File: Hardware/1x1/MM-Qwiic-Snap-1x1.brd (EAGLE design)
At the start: 80 x 34.3 mm, 57 parts, among them J15 MICROMOD-2222-C, J2 QWIIC_RIGHT_ANGLE, U1 MCP73831, U5 AP7361C-33FGEUDFN-8

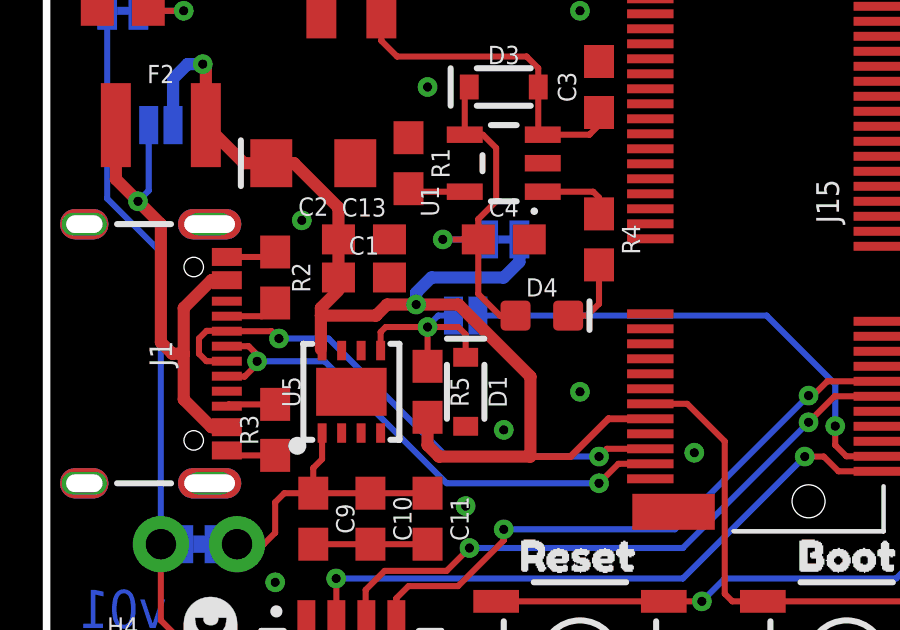
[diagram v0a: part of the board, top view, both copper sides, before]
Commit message: Create 2x1 version and generate production files
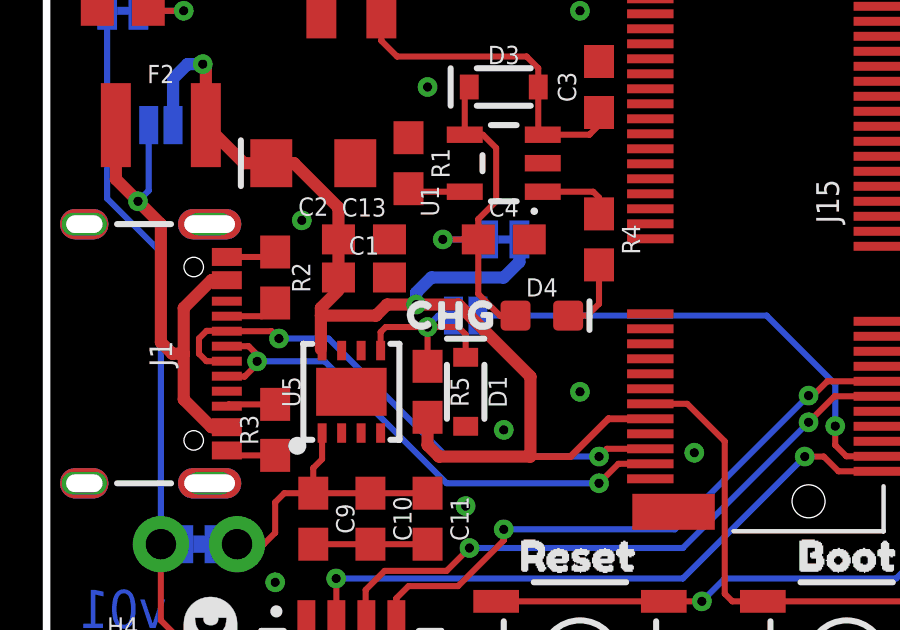
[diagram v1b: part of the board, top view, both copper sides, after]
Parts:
- added U$4: (no value), output:CHG0
- added U$5: (no value), output:#VIN#0
- added U$6: (no value), output:#3#3V#0
- added U$7: (no value), output:#BYP#0
- added U$8: (no value), output:#VE#0
- added U$9: (no value), output:#MEAS#0
- moved LOGO1 7.62 mm to (31.8, 19.1)
- moved LOGO3 7.62 mm to (31.6, 9.65)
- moved U$68 7.62 mm to (31.8, 15.2)
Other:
- board text removed: "Selective Solder Nozzle Width: 0.354331"
- board text removed: "in"
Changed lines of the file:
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@@
 <?xml version="1.0" encoding="utf-8"?>
 <!DOCTYPE eagle SYSTEM "eagle.dtd">
-<eagle version="9.5.2">
+<eagle version="9.6.2">
 <drawing>
 <settings>
@@
 <layer number="23" name="tOrigins" color="15" fill="1" visible="yes" active="yes"/>
 <layer number="24" name="bOrigins" color="15" fill="1" visible="yes" active="yes"/>
-<layer number="25" name="tNames" color="7" fill="1" visible="no" active="yes"/>
-<layer number="26" name="bNames" color="7" fill="1" visible="no" active="yes"/>
-<layer number="27" name="tValues" color="7" fill="1" visible="no" active="yes"/>
-<layer number="28" name="bValues" color="7" fill="1" visible="no" active="yes"/>
-<layer number="29" name="tStop" color="7" fill="3" visible="no" active="yes"/>
-<layer number="30" name="bStop" color="7" fill="6" visible="no" active="yes"/>
-<layer number="31" name="tCream" color="7" fill="4" visible="no" active="yes"/>
-<layer number="32" name="bCream" color="7" fill="5" visible="no" active="yes"/>
-<layer number="33" name="tFinish" color="6" fill="3" visible="no" active="yes"/>
-<layer number="34" name="bFinish" color="6" fill="6" visible="no" active="yes"/>
-<layer number="35" name="tGlue" color="7" fill="4" visible="no" active="yes"/>
-<layer number="36" name="bGlue" color="7" fill="5" visible="no" active="yes"/>
-<layer number="37" name="tTest" color="7" fill="1" visible="no" active="yes"/>
-<layer number="38" name="bTest" color="7" fill="1" visible="no" active="yes"/>
-<layer number="39" name="tKeepout" color="4" fill="11" visible="no" active="yes"/>
-<layer number="40" name="bKeepout" color="1" fill="11" visible="no" active="yes"/>
-<layer number="41" name="tRestrict" color="4" fill="10" visible="no" active="yes"/>
-<layer number="42" name="bRestrict" color="1" fill="10" visible="no" active="yes"/>
-<layer number="43" name="vRestrict" color="2" fill="10" visible="no" active="yes"/>
-<layer number="44" name="Drills" color="7" fill="1" visible="no" active="yes"/>
+<layer number="25" name="tNames" color="7" fill="1" visible="yes" active="yes"/>
+<layer number="26" name="bNames" color="7" fill="1" visible="yes" active="yes"/>
+<layer number="27" name="tValues" color="7" fill="1" visible="yes" active="yes"/>
+<layer number="28" name="bValues" color="7" fill="1" visible="yes" active="yes"/>
+<layer number="29" name="tStop" color="7" fill="3" visible="yes" active="yes"/>
+<layer number="30" name="bStop" color="7" fill="6" visible="yes" active="yes"/>
+<layer number="31" name="tCream" color="7" fill="4" visible="yes" active="yes"/>
+<layer number="32" name="bCream" color="7" fill="5" visible="yes" active="yes"/>
+<layer number="33" name="tFinish" color="6" fill="3" visible="yes" active="yes"/>
+<layer number="34" name="bFinish" color="6" fill="6" visible="yes" active="yes"/>
+<layer number="35" name="tGlue" color="7" fill="4" visible="yes" active="yes"/>
+<layer number="36" name="bGlue" color="7" fill="5" visible="yes" active="yes"/>
+<layer number="37" name="tTest" color="7" fill="1" visible="yes" active="yes"/>
+<layer number="38" name="bTest" color="7" fill="1" visible="yes" active="yes"/>
+<layer number="39" name="tKeepout" color="4" fill="11" visible="yes" active="yes"/>
+<layer number="40" name="bKeepout" color="1" fill="11" visible="yes" active="yes"/>
+<layer number="41" name="tRestrict" color="4" fill="10" visible="yes" active="yes"/>
+<layer number="42" name="bRestrict" color="1" fill="10" visible="yes" active="yes"/>
+<layer number="43" name="vRestrict" color="2" fill="10" visible="yes" active="yes"/>
+<layer number="44" name="Drills" color="7" fill="1" visible="yes" active="yes"/>
 <layer number="45" name="Holes" color="7" fill="1" visible="yes" active="yes"/>
-<layer number="46" name="Milling" color="3" fill="1" visible="no" active="yes"/>
-<layer number="47" name="Measures" color="7" fill="1" visible="no" active="yes"/>
-<layer number="48" name="Document" color="7" fill="1" visible="no" active="yes"/>
-<layer number="49" name="Reference" color="7" fill="1" visible="no" active="yes"/>
-<layer number="50" name="dxf" color="7" fill="1" visible="no" active="yes"/>
+<layer number="46" name="Milling" color="3" fill="1" visible="yes" active="yes"/>
+<layer number="47" name="Measures" color="7" fill="1" visible="yes" active="yes"/>
+<layer number="48" name="Document" color="7" fill="1" visible="yes" active="yes"/>
+<layer number="49" name="Reference" color="7" fill="1" visible="yes" active="yes"/>
+<layer number="50" name="dxf" color="7" fill="1" visible="yes" active="yes"/>
 <layer number="51" name="tDocu" color="6" fill="1" visible="yes" active="yes"/>
-<layer number="52" name="bDocu" color="7" fill="1" visible="no" active="yes"/>
+<layer number="52" name="bDocu" color="7" fill="1" visible="yes" active="yes"/>
 <layer number="91" name="Nets" color="2" fill="1" visible="no" active="no"/>
 <layer number="92" name="Busses" color="1" fill="1" visible="no" active="no"/>
@@
 <wire x1="41.783" y1="47.244" x2="41.783" y2="46.863" width="0.2032" layer="41"/>
 <text x="36.83" y="-21.59" size="1.778" layer="51" font="vector" ratio="15">Priyanka Makin</text>
-<wire x1="58.42" y1="50.8" x2="58.42" y2="40.64" width="9.00000625" layer="48"/>
-<wire x1="58.42" y1="40.64" x2="55.88" y2="35.56" width="9.00000625" layer="48"/>
-<wire x1="55.88" y1="35.56" x2="55.88" y2="12.7" width="9.00000625" layer="48"/>
-<text x="71.12" y="40.64" size="1.778" layer="48" font="vector" ratio="15">Selective Solder Nozzle Width:
-0.354331</text>
-<dimension x1="2.54" y1="55.88" x2="64.77" y2="55.88" x3="33.655" y3="60.96" textsize="1.778" textratio="15" layer="47" unit="inch"/>
-<dimension x1="64.77" y1="55.88" x2="64.77" y2="2.54" x3="74.93" y3="29.21" textsize="1.778" textratio="15" layer="47" unit="inch"/>
-<text x="36.83" y="66.548" size="1.778" layer="47" font="vector" ratio="15">in</text>
-<text x="78.105" y="32.512" size="1.778" layer="47" font="vector" ratio="15" rot="R90">in</text>
-<text x="74.295" y="32.512" size="1.778" layer="47" font="vector" ratio="15" rot="R90">in</text>
-<text x="38.608" y="63.246" size="1.778" layer="47" font="vector" ratio="15" rot="R180">in</text>
-<dimension x1="0" y1="58.42" x2="67.31" y2="58.42" x3="33.655" y3="66.04" textsize="1.778" textratio="15" layer="47" unit="inch"/>
-<dimension x1="67.31" y1="58.42" x2="67.31" y2="0" x3="78.74" y3="29.21" textsize="1.778" textratio="15" layer="47" unit="inch"/>
 </plain>
 <attributes>
@@
 <element name="U$19" library="buzzard_labels (10)" package="BOOT2" value="" x="24.13" y="7.239" smashed="yes"/>
 <element name="LOGO2" library="SparkFun-Aesthetics" package="QWIIC_5.5MM" value="QWIIC_LOGO_CONNECTOR" x="5.461" y="3.1115" smashed="yes" rot="R90"/>
-<element name="LOGO3" library="SparkFun-Aesthetics" package="OSHW-LOGO-M" value="OSHW-LOGOM" x="24.003" y="9.652" smashed="yes" rot="MR0"/>
+<element name="LOGO3" library="SparkFun-Aesthetics" package="OSHW-LOGO-M" value="OSHW-LOGOM" x="31.623" y="9.652" smashed="yes" rot="MR0"/>
 <element name="U$55" library="buzzard_labels (9)" package="22229" value="" x="28.232" y="31.12" smashed="yes"/>
 <element name="H5" library="SparkFun-Hardware" package="STAND-OFF-REFLOW-M2.5" value="STAND-OFF-REFLOW2.5MM_TALL" x="45.47" y="15.03" smashed="yes">
@@
 <attribute name="VALUE" x="24.765" y="19.05" size="0.762" layer="27" rot="R270" align="center"/>
 </element>
-<element name="LOGO1" library="SparkFun-Aesthetics" package="SFE_LOGO_NAME_FLAME_.2" value="SFE_LOGO_NAME_FLAME.2_INCH" x="24.13" y="19.05" smashed="yes" rot="MR0"/>
+<element name="LOGO1" library="SparkFun-Aesthetics" package="SFE_LOGO_NAME_FLAME_.2" value="SFE_LOGO_NAME_FLAME.2_INCH" x="31.75" y="19.05" smashed="yes" rot="MR0"/>
 <element name="U$1" library="buzzard_labels (5)" package="3V31" value="" x="0.635" y="28.575" smashed="yes"/>
 <element name="U$44" library="SparkFun-Aesthetics" package="SFE_LOGO_FLAME_.2" value="" x="16.764" y="29.845" smashed="yes"/>
 <element name="U$67" library="SparkFun-MicroMod" package="MICROMOD_LOGO_.5" value="" x="62.103" y="32.131" smashed="yes"/>
-<element name="U$68" library="SparkFun-MicroMod" package="MICROMOD_LOGO_.5" value="" x="24.13" y="15.24" smashed="yes" rot="MR0"/>
+<element name="U$68" library="SparkFun-MicroMod" package="MICROMOD_LOGO_.5" value="" x="31.75" y="15.24" smashed="yes" rot="MR0"/>
 <element name="J2" library="SparkFun-Connectors" package="JST04_1MM_RA" value="QWIIC_RIGHT_ANGLE" x="10.16" y="5.08" smashed="yes">
 <attribute name="NAME" x="8.763" y="2.921" size="0.6096" layer="25" font="vector" ratio="20"/>
@@
 <attribute name="PROD_ID" value="HW-14899" x="72.39" y="25.4" size="1.778" layer="27" font="vector" ratio="15" display="off"/>
 </element>
+<element name="U$4" library="output" package="CHG0" value="" x="11.303" y="15.24" smashed="yes"/>
+<element name="U$6" library="output" package="#3#3V#0" value="" x="8.255" y="25.4" smashed="yes" rot="MR0"/>
+<element name="U$7" library="output" package="#BYP#0" value="" x="8.89" y="21.59" smashed="yes" rot="MR0"/>
+<element name="U$9" library="output" package="#MEAS#0" value="" x="12.319" y="7.62" smashed="yes" rot="MR0"/>
+<element name="U$5" library="output" package="#VIN#0" value="" x="14.351" y="17.78" smashed="yes" rot="MR0"/>
+<element name="U$8" library="output" package="#VE#0" value="" x="13.208" y="15.24" smashed="yes" rot="MR0"/>
 </elements>
 <signals>
@@
 </drawing>
 <compatibility>
-<note version="6.3" minversion="6.2.2" severity="warning">
-Since Version 6.2.2 text objects can contain more than one line,
-which will not be processed correctly with this version.
-</note>
 <note version="8.3" severity="warning">
 Since Version 8.3, EAGLE supports URNs for individual library
